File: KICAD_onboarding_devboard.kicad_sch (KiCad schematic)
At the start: 2 parts, among them U1 STM32G0B1KETx

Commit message: bruh
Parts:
- added C?: 100nF, symbol Device:C
- added D?: D_TVS_Dual_AAC, symbol Device:D_TVS_Dual_AAC
- added FL?: Choke_Coilcraft_0603USB-142, Inductor_SMD:L_CommonModeChoke_Coilcraft_0603USB, symbol Filter:Choke_Coilcraft_0603USB-142
- added J? (x2): RJ45, symbol Connector:RJ45
- added R?: 120R, symbol Device:R
- added U?: ISO1050DUB, Package_SO:SOP-8_6.62x9.15mm_P2.54mm, symbol Interface_CAN_LIN:ISO1050DUB
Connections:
- net FDCAN_RX: now also U?.2 (RXD)
- net FDCAN_TX: now also U?.3 (TXD)
- net GND: now also C?.2, U?.4 (GND1)
- new net: FL?.2, U?.6 (CANL)
- new net: FL?.3, U?.7 (CANH)
- new net: J?.4, J?.4
- new net: J?.5, J?.5
- new net: J?.7, J?.7
- new net: J?.8, J?.8
- new net CAN_3.3V: C?.1, U?.1 (VCC1)
- new net CAN_5V: J?.3, J?.3, U?.8 (VCC2)
- new net CAN_GND: D?.3 (common), J?.6, J?.6, U?.5 (GND2)
- new net CAN_H: D?.2 (A2), FL?.4, J?.1, J?.1, R?.1
- new net CAN_L: D?.1 (A1), FL?.1, J?.2, J?.2, R?.2
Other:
- note added: "CANBUS"
- note added: "need: switchable 5V power (isolated?) get correct part for inductor or w/e"

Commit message: this serial adapter finna be funk
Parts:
- removed R?: 120R, symbol Device:R
- added R?: 120R, symbol Device:R
- added SW? (x2): SW_SPST, symbol Switch:SW_SPST
- added U?: FT232RL, Package_SO:SSOP-28_5.3x10.2mm_P0.65mm, symbol Interface_USB:FT232RL
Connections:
- net CAN_3.3V is gone; now on net 3.3V: C?.1, U?.1 (VCC1)
- net CAN_5V: now also SW?.1 (A)
- net CAN_H: now also SW?.1 (A)
- net CAN_L: now also R?.2
- net GND: now also J?.5 (GND), J?.6 (Shield)
- new net: R?.1, SW?.2 (B)
- new net 5V: SW?.2 (B)
- no-connect marks 0 -> 1
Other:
- note added: "need: swap out inductor for real part (snapEDA isn't real bruh)"
- note removed: "need: switchable 5V power (isolated?) get correct part for inductor or w/e"
- moved on the sheet: C?, D?, FL?, J?, U1, U?

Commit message: b
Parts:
- added U?: MCP2200-I-SO, Package_SO:SOIC-20W_7.5x12.8mm_P1.27mm, symbol Interface_USB:MCP2200-I-SO
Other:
- moved on the sheet: U?
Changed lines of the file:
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@@
 	)
 	(symbol
-		(lib_id "Interface_USB:FT232RL")
-		(at 77.47 44.45 0)
+		(lib_id "Interface_USB:MCP2200-I-SO")
+		(at 138.43 44.45 0)
 		(unit 1)
 		(exclude_from_sim no)
@@
 		(fields_autoplaced yes)
 		(property "Reference" "U?"
-			(at 82.2041 17.78 0)
+			(at 140.6241 64.77 0)
+			(effects
+				(font
+					(size 1.27 1.27)
+				)
+				(justify left)
+			)
+		)
+		(property "Value" "MCP2200-I-SO"
+			(at 140.6241 67.31 0)
+			(effects
+				(font
+					(size 1.27 1.27)
+				)
+				(justify left)
+			)
+		)
+		(property "Footprint" "Package_SO:SOIC-20W_7.5x12.8mm_P1.27mm"
+			(at 138.43 73.66 0)
+			(effects
+				(font
+					(size 1.27 1.27)
+				)
+				(hide yes)
+			)
+		)
+		(property "Datasheet" "http://ww1.microchip.com/downloads/en/DeviceDoc/200022228D.pdf"
+			(at 138.43 69.85 0)
+			(effects
+				(font
+					(size 1.27 1.27)
+				)
+				(hide yes)
+			)
+		)
+		(property "Description" "USB 2.0 to UART Protocol Converter with GPIO, SOIC-20"
+			(at 138.43 44.45 0)
+			(effects
+				(font
+					(size 1.27 1.27)
+				)
+				(hide yes)
+			)
+		)
+		(pin "6"
+		)
+		(pin "3"
+		)
+		(pin "15"
+		)
+		(pin "2"
+		)
+		(pin "1"
+		)
+		(pin "14"
+		)
+		(pin "8"
+		)
+		(pin "9"
+		)
+		(pin "19"
+		)
+		(pin "17"
+		)
+		(pin "10"
+		)
+		(pin "7"
+		)
+		(pin "4"
+		)
+		(pin "5"
+		)
+		(pin "20"
+		)
+		(pin "12"
+		)
+		(pin "11"
+		)
+		(pin "16"
+		)
+		(pin "18"
+		)
+		(pin "13"
+		)
+		(instances
+			(project ""
+				(path "/8af9afbd-1b65-47c4-8f98-8f2b7f674f49"
+					(reference "U?")
+					(unit 1)
+				)
+			)
+		)
+	)
+	(symbol
+		(lib_id "Interface_USB:FT232RL")
+		(at 82.55 43.18 0)
+		(unit 1)
+		(exclude_from_sim no)
+		(in_bom yes)
+		(on_board yes)
+		(dnp no)
+		(fields_autoplaced yes)
+		(property "Reference" "U?"
+			(at 87.2841 16.51 0)
 			(effects
 				(font
@@
 		)
 		(property "Value" "FT232RL"
-			(at 82.2041 20.32 0)
+			(at 87.2841 19.05 0)
 			(effects
 				(font
@@
 		)
 		(property "Footprint" "Package_SO:SSOP-28_5.3x10.2mm_P0.65mm"
-			(at 105.41 67.31 0)
+			(at 110.49 66.04 0)
 			(effects
 				(font
@@
 		)
 		(property "Datasheet" "https://www.ftdichip.com/Support/Documents/DataSheets/ICs/DS_FT232R.pdf"
-			(at 77.47 44.45 0)
+			(at 82.55 43.18 0)
 			(effects
 				(font
@@
 		)
 		(property "Description" "USB to Serial Interface, SSOP-28"
-			(at 77.47 44.45 0)
+			(at 82.55 43.18 0)
 			(effects
 				(font

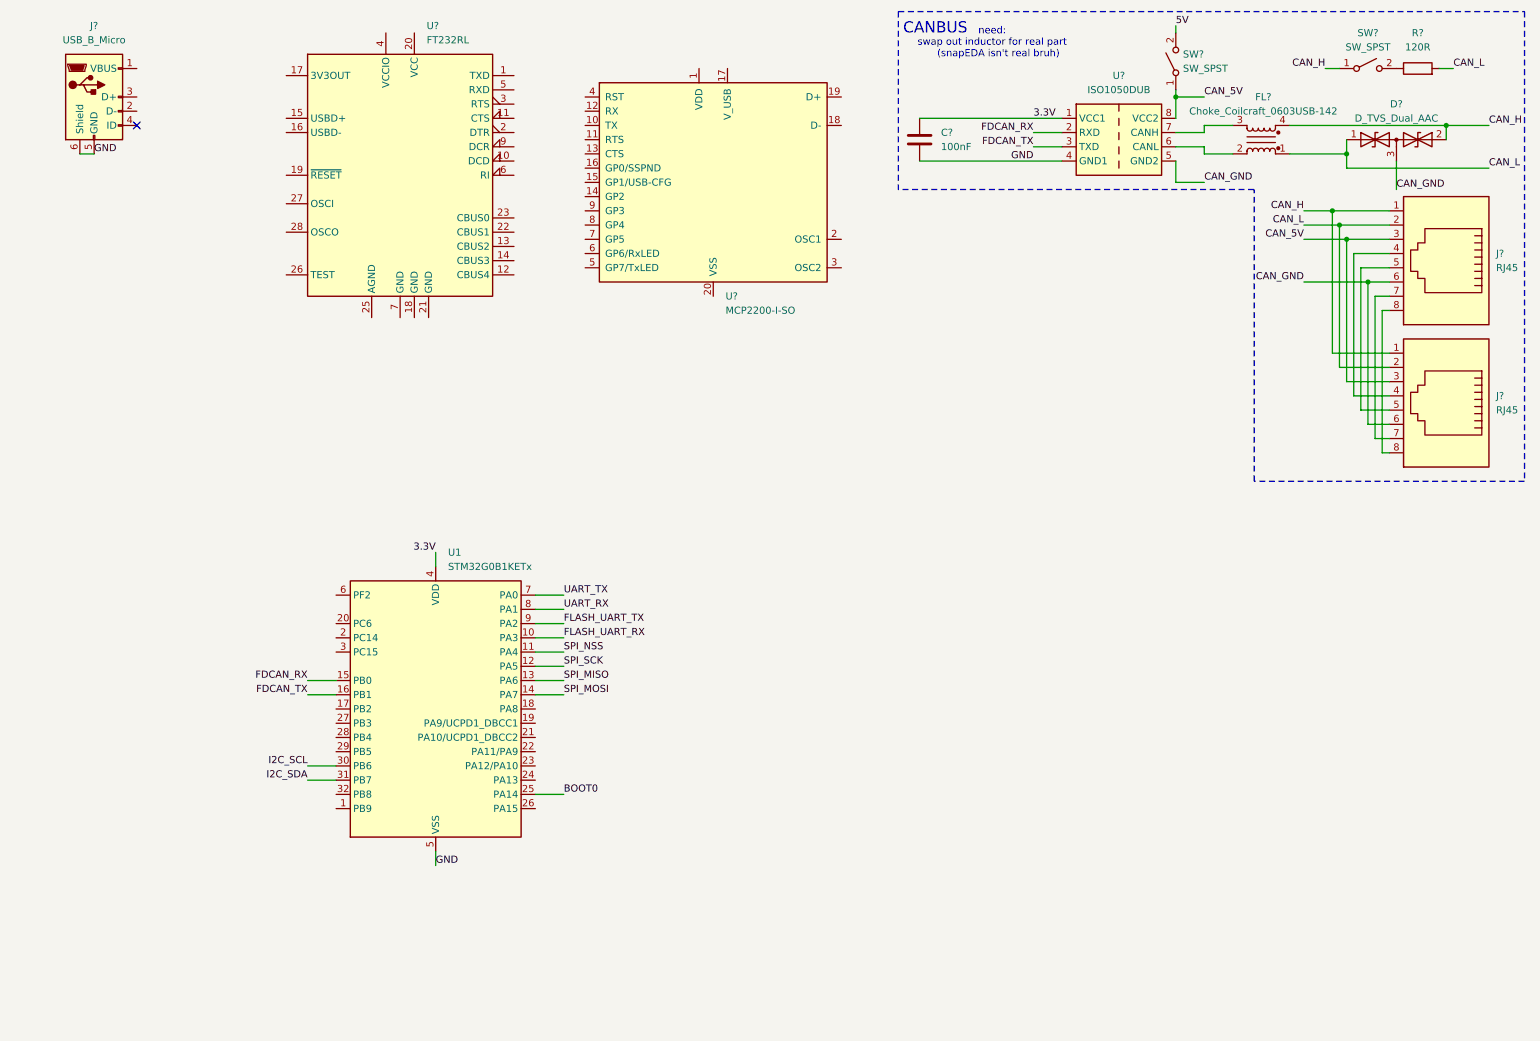
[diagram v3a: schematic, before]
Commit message: potentially finished uart+stlink
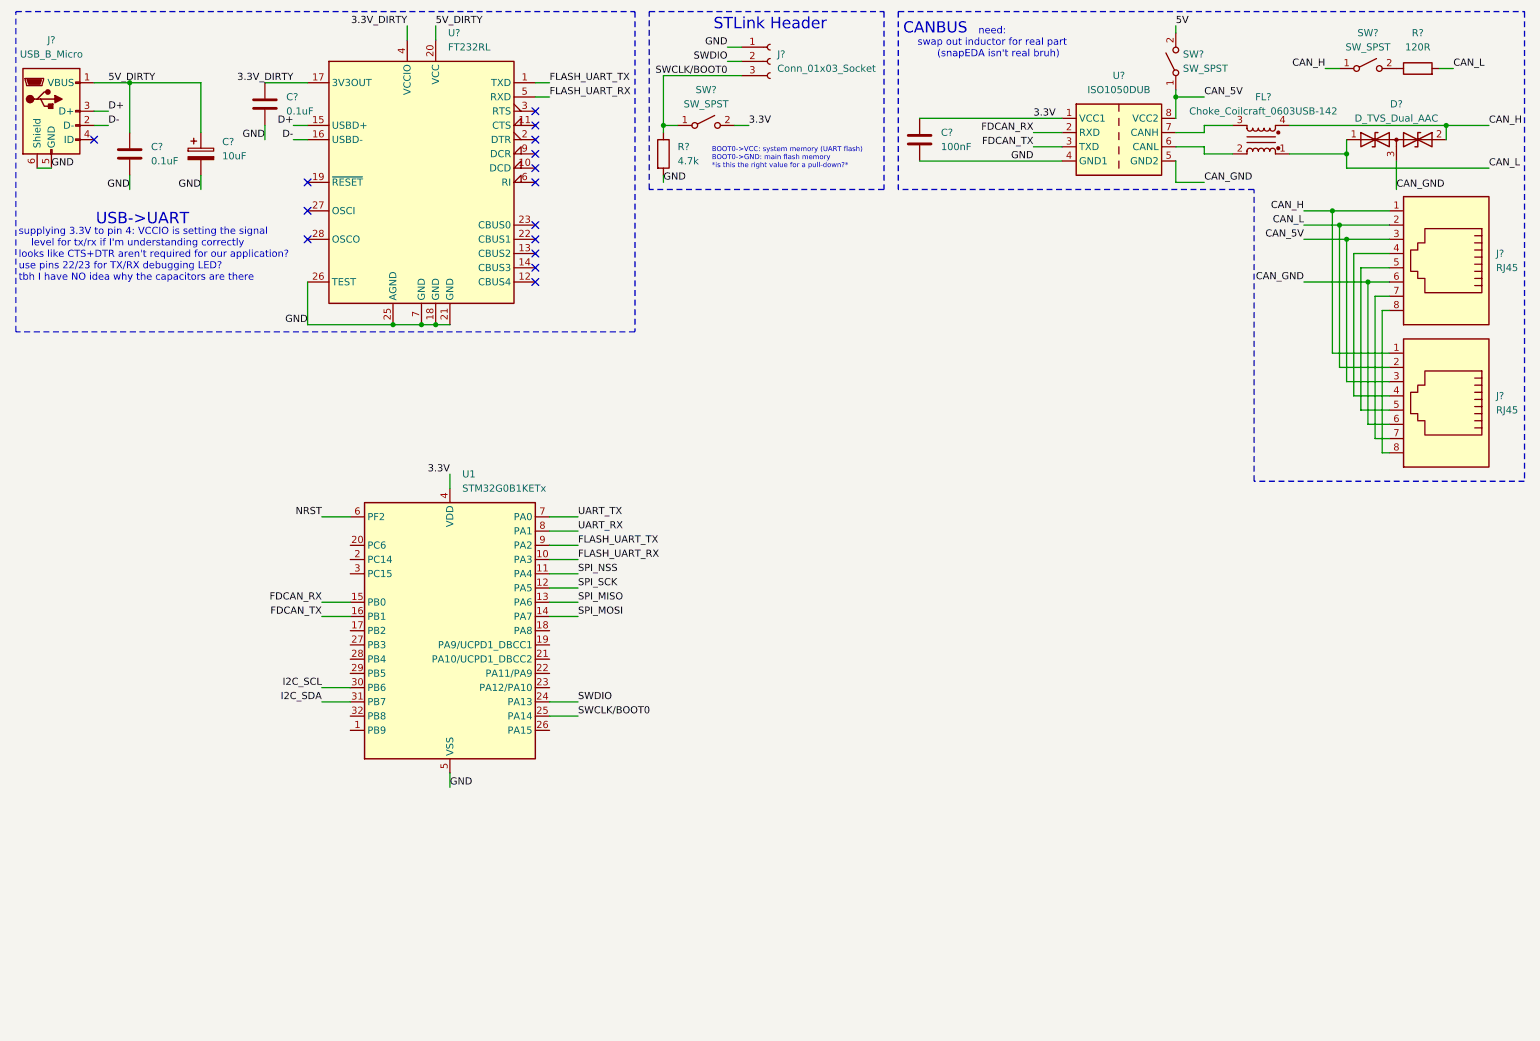
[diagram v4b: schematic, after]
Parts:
- removed U?: MCP2200-I-SO, Package_SO:SOIC-20W_7.5x12.8mm_P1.27mm, symbol Interface_USB:MCP2200-I-SO
- removed U?: FT232RL, Package_SO:SSOP-28_5.3x10.2mm_P0.65mm, symbol Interface_USB:FT232RL
- added C?: 10uF, symbol Device:C_Polarized
- added C? (x2): 0.1uF, symbol Device:C
- added J?: Conn_01x03_Socket, symbol Connector:Conn_01x03_Socket
- added R?: 4.7k, symbol Device:R
- added SW?: SW_SPST, symbol Switch:SW_SPST
- added U?: FT232RL, Package_SO:SSOP-28_5.3x10.2mm_P0.65mm, symbol Interface_USB:FT232RL
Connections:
- net 3.3V: now also SW?.2 (B)
- net FLASH_UART_RX: now also U?.5 (RXD)
- net FLASH_UART_TX: now also U?.1 (TXD)
- net GND: now also C?.2, C?.2, C?.2, J?.1 (Pin_1), R?.2, U?.18 (GND), U?.21 (GND), U?.25 (AGND), U?.26 (TEST), U?.7 (GND)
- net 5V_DIRTY: now reaches J?.1 (VBUS)
- net 5V_DIRTY: now also C?.1, C?.1, U?.20 (VCC)
- net D-: now reaches J?.2 (D-)
- net D-: now also U?.16 (USBD-)
- net D+: now reaches J?.3 (D+)
- net D+: now also U?.15 (USBD+)
- net SWDIO: now reaches U1.24 (PA13)
- net SWDIO: now also J?.2 (Pin_2)
- net NRST: now reaches U1.6 (PF2)
- net BOOT0 renamed SWCLK/BOOT0
- net SWCLK/BOOT0: now also J?.3 (Pin_3), R?.1, SW?.1 (A)
- new net 3.3V_DIRTY: C?.1, U?.17 (3V3OUT), U?.4 (VCCIO)
- no-connect marks 1 -> 15
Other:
- note added: "BOOT0->VCC: system memory (UART flash) BOOT0->GND: main flash memory *is this the right value for a pull-down?*"
- note added: "STLink Header"
- note added: "USB->UART"
- note added: "supplying 3.3V to pin 4: VCCIO is setting the signal level for tx/rx if I'm understanding correctly looks like CTS+DTR aren't required for our application? use pins 22/23 for TX/RX debugging LED? tbh I have NO idea why the capacitors are there"
- moved on the sheet: J?, U1

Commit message: idk what I changed
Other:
- note added: "*I don't think this connector is right...*"
- note added: "BOOT0->VCC: system memory (UART flash) BOOT0->GND: main flash memory *is this the right value for a pull-down?* *should it be a pull-up?*"
- note added: "headers needed: 1. SPI_NSS X 2. SPI_SCK X 3. SPI_MISO X 4. SPI_MOSI X 5. UART_TX X 6. UART_RX X 7. I2C_SCL 8. I2C_SDA 9. 3.3V 10. 5V? 11. GND 12. extra pins for shtuff"
- note added: "supplying 3.3V to pin 4: VCCIO is setting the signal level for tx/rx if I'm understanding correctly looks like CTS+DTR aren't required for our application? use pins 22/23 for TX/RX debugging LED?"
- note removed: "BOOT0->VCC: system memory (UART flash) BOOT0->GND: main flash memory *is this the right value for a pull-down?*"
- note removed: "supplying 3.3V to pin 4: VCCIO is setting the signal level for tx/rx if I'm understanding correctly looks like CTS+DTR aren't required for our application? use pins 22/23 for TX/RX debugging LED? tbh I have NO idea why the capacitors are there"
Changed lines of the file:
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@@
 		)
 	)
-	(text "BOOT0->VCC: system memory (UART flash)\nBOOT0->GND: main flash memory\n*is this the right value for a pull-down?*\n"
+	(text "*I don't think this\nconnector is right...*"
+		(exclude_from_sim no)
+		(at 159.766 21.336 0)
+		(effects
+			(font
+				(size 0.6 0.6)
+			)
+		)
+	)
+	(text "BOOT0->VCC: system memory (UART flash)\nBOOT0->GND: main flash memory\n*is this the right value for a pull-down?*\n	*should it be a pull-up?*"
 		(exclude_from_sim no)
 		(at 138.176 40.132 0)
@@
 		)
 	)
+	(text "headers needed:\n1. SPI_NSS			X\n2. SPI_SCK			X\n3. SPI_MISO			X\n4. SPI_MOSI			X\n5. UART_TX			X\n6. UART_RX 			X\n7. I2C_SCL\n8. I2C_SDA\n9. 3.3V\n10. 5V?\n11. GND\n12. extra pins for shtuff"
+		(exclude_from_sim no)
+		(at 173.99 112.014 0)
+		(effects
+			(font
+				(size 1.27 1.27)
+			)
+			(justify left)
+		)
+	)
 	(text "USB->UART"
 		(exclude_from_sim no)
-		(at 36.576 51.054 0)
+		(at 36.83 49.276 0)
 		(effects
 			(font
@@
 		)
 	)
-	(text "supplying 3.3V to pin 4: VCCIO is setting the signal\n	level for tx/rx if I'm understanding correctly\nlooks like CTS+DTR aren't required for our application?\nuse pins 22/23 for TX/RX debugging LED? \ntbh I have NO idea why the capacitors are there\n"
+	(text "supplying 3.3V to pin 4: VCCIO is setting the signal\n	level for tx/rx if I'm understanding correctly\nlooks like CTS+DTR aren't required for our application?\nuse pins 22/23 for TX/RX debugging LED?"
 		(exclude_from_sim no)
-		(at 14.478 57.404 0)
+		(at 14.732 55.626 0)
 		(effects
 			(font

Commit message: beans
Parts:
- added U?: TLV76133DCY, Package_TO_SOT_SMD:SOT-223-3_TabPin2, symbol Regulator_Linear:TLV76133DCY
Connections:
- net 3.3V: now also U?.2 (VO)
- net 3.3V_DIRTY: now also U?.3 (VI)
- net GND: now also U?.1 (GND)
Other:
- note added: "*is there a 3.3->3.3 version? or a 5->3.3 version?*"
- note added: "TODO: -HEADERS for SPI,UART,I2C,3.3,5,GND, and spare IO -I2C hardware? Unsure what else I'd need if there's no buffer chip -CAN inductor swap -more power protection!? coupling capacitors? not sure how to go about that stuff I'm aware of: -consider uart_flash tx/rx LEDs -consider disconnecting flash_uart when using STlink, I might have missed a component for STlink but I think I have the pins I ne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"
- note removed: "headers needed: 1. SPI_NSS X 2. SPI_SCK X 3. SPI_MISO X 4. SPI_MOSI X 5. UART_TX X 6. UART_RX X 7. I2C_SCL 8. I2C_SDA 9. 3.3V 10. 5V? 11. GND 12. extra pins for shtuff"
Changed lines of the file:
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@@
+	(wire
+		(pts
+			(xy 151.13 64.77) (xy 151.13 67.31)
+		)
+		(stroke
+			(width 0)
+			(type default)
+		)
+	)
 	(wire
 		(pts
@@
 	(wire
 		(pts
+			(xy 158.75 57.15) (xy 161.29 57.15)
+		)
+		(stroke
+			(width 0)
+			(type default)
+		)
+	)
+	(wire
+		(pts
 			(xy 220.98 44.45) (xy 226.06 44.45)
 		)
@@
 		(pts
 			(xy 106.68 26.67) (xy 109.22 26.67)
+		)
+		(stroke
+			(width 0)
+			(type default)
+		)
+	)
+	(wire
+		(pts
+			(xy 140.97 57.15) (xy 143.51 57.15)
 		)
 		(stroke
@@
 		)
 	)
+	(text "*is there a 3.3->3.3 version? \n	or a 5->3.3 version?*"
+		(exclude_from_sim no)
+		(at 174.498 62.992 0)
+		(effects
+			(font
+				(size 1.27 1.27)
+			)
+		)
+	)
 	(text "*I don't think this\nconnector is right...*"
 		(exclude_from_sim no)
@@
 		)
 	)
-	(text "headers needed:\n1. SPI_NSS			X\n2. SPI_SCK			X\n3. SPI_MISO			X\n4. SPI_MOSI			X\n5. UART_TX			X\n6. UART_RX 			X\n7. I2C_SCL\n8. I2C_SDA\n9. 3.3V\n10. 5V?\n11. GND\n12. extra pins for shtuff"
+	(text "TODO:\n-HEADERS for SPI,UART,I2C,3.3,5,GND, and spare IO\n-I2C hardware? Unsure what else I'd need if there's no buffer chip\n-CAN inductor swap\n-more power protection!? coupling capacitors? not sure how to go about that\n\nstuff I'm aware of:\n-consider uart_flash tx/rx LEDs \n-consider disconnecting flash_uart when using STlink, I might have missed\n	a component for STlink but I think I have the pins I need....\n"
 		(exclude_from_sim no)
-		(at 173.99 112.014 0)
-		(effects
-			(font
-				(size 1.27 1.27)
+		(at 147.066 113.03 0)
+		(effects
+			(font
+				(size 1.524 1.524)
 			)
 			(justify left)
@@
 		)
 	)
+	(label "3.3V_DIRTY"
+		(at 140.97 57.15 180)
+		(fields_autoplaced yes)
+		(effects
+			(font
+				(size 1.27 1.27)
+			)
+			(justify right bottom)
+		)
+	)
 	(label "SWCLK{slash}BOOT0"
 		(at 140.97 25.4 180)
@@
 		)
 	)
+	(label "3.3V"
+		(at 161.29 57.15 0)
+		(fields_autoplaced yes)
+		(effects
+			(font
+				(size 1.27 1.27)
+			)
+			(justify left bottom)
+		)
+	)
 	(label "CAN_L"
 		(at 243.84 52.07 180)
@@
 	(label "SWDIO"
 		(at 114.3 137.16 0)
+		(fields_autoplaced yes)
+		(effects
+			(font
+				(size 1.27 1.27)
+			)
+			(justify left bottom)
+		)
+	)
+	(label "GND"
+		(at 151.13 67.31 0)
 		(fields_autoplaced yes)
 		(effects
@@
 					(unit 1)
 				)
+			)
+		)
+	)
+	(symbol
+		(lib_id "Regulator_Linear:TLV76133DCY")
+		(at 151.13 57.15 0)
+		(unit 1)
+		(exclude_from_sim no)
+		(in_bom yes)
+		(on_board yes)
+		(dnp no)
+		(fields_autoplaced yes)
+		(property "Reference" "U?"
+			(at 151.13 50.8 0)
+			(effects
+				(font
+					(size 1.27 1.27)
+				)
+			)
+		)
+		(property "Value" "TLV76133DCY"
+			(at 151.13 53.34 0)
+			(effects
+				(font
+					(size 1.27 1.27)
+				)
+			)
+		)
+		(property "Footprint" "Package_TO_SOT_SMD:SOT-223-3_TabPin2"
+			(at 151.13 68.58 0)
+			(effects
+				(font
+					(size 1.27 1.27)
+				)
+				(hide yes)
+			)
+		)
+		(property "Datasheet" "https://www.ti.com/lit/ds/symlink/tlv761.pdf"
+			(at 151.13 71.12 0)
+			(effects
+				(font
+					(size 1.27 1.27)
+				)
+				(hide yes)
+			)
+		)
+		(property "Description" "3.3V, 1A, Low Noise, High-PSRR LDO Regulator, 2.5V...16V input, SOT-223"
+			(at 151.13 57.15 0)
+			(effects
+				(font
+					(size 1.27 1.27)
+				)
+				(hide yes)
+			)
+		)
+		(pin "3"
+		)
+		(pin "1"
+		)
+		(pin "2"
+		)
+		(instances
+			(project ""
+				(path "/8af9afbd-1b65-47c4-8f98-8f2b7f674f49"
+					(reference "U?")
+					(unit 1)
+				)

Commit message: br
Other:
- note added: "*is there a 5->3.3 version? this seems too simple but from the datasheet it seemed like it was just this...?*"
- note removed: "*is there a 3.3->3.3 version? or a 5->3.3 version?*"
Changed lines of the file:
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@@
 		)
 	)
-	(text "*is there a 3.3->3.3 version? \n	or a 5->3.3 version?*"
+	(text "*is there a 5->3.3 version? this seems too simple\n	but from the datasheet it seemed like it was just this...?*"
 		(exclude_from_sim no)
-		(at 174.498 62.992 0)
+		(at 192.278 62.992 0)
 		(effects
 			(font

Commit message: a
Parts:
- removed U1: STM32G0B1KETx, Package_QFP:LQFP-32_7x7mm_P0.8mm, symbol MCU_ST_STM32G0:STM32G0B1KETx
- added U?: STM32G0B1CBTx, Package_QFP:LQFP-48_7x7mm_P0.5mm, symbol MCU_ST_STM32G0:STM32G0B1CBTx
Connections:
- net 3.3V: now also U?.6 (VDD)
- net FLASH_UART_RX: now also U?.14 (PA3)
- net FLASH_UART_TX: now also U?.13 (PA2)
- net GND: now also U?.7 (VSS)
- net NRST: now also U?.10 (PF2)
- net SWCLK/BOOT0: now also U?.36 (PA14)
- net SWDIO: now also U?.35 (PA13)
- new net FDCAN1_RX: U?.47 (PB8)
- new net FDCAN1_TX: U?.48 (PB9)
- new net I2C1_SCL: U?.45 (PB6)
- new net I2C1_SDA: U?.46 (PB7)
- new net SPI2_MISO: U?.26 (PB14)
- new net SPI2_MOSI: U?.27 (PB15)
- new net SPI2_NSS: U?.24 (PB12)
- new net SPI2_SCK: U?.25 (PB13)
- new net USART4_RX: U?.12 (PA1)
- new net USART4_TX: U?.11 (PA0)
- no-connect marks 15 -> 17
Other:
- note added: "TODO: CAN - isolated DC-DC converter for 5V POWER - "smart switch" where board is supplied either 5V or 12V power (phoenix block for 12V) - LDO needs caps and stuff according to TI spec *use an isolated DC-DC before stepping down to 3.3 to clean up source* BOOT - BOOT0/SWCLK needs resistor to ground and pushbutton to 3.3V - NRST needs button to pull to ground, else leave high - STLink connector i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"
- note removed: "*is there a 5->3.3 version? this seems too simple but from the datasheet it seemed like it was just this...?*"
- note removed: "TODO: -HEADERS for SPI,UART,I2C,3.3,5,GND, and spare IO -I2C hardware? Unsure what else I'd need if there's no buffer chip -CAN inductor swap -more power protection!? coupling capacitors? not sure how to go about that stuff I'm aware of: -consider uart_flash tx/rx LEDs -consider disconnecting flash_uart when using STlink, I might have missed a component for STlink but I think I have the pins I ne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"
